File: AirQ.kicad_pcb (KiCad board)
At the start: 2 copper layers, 1 part, among them U1 ESP32-H2-MINI-1-H2

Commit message: changes
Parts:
- added D1: SS12, Diode_SMD:D_SMA, F.Cu at (130.0, 106.5)
- added U2: AP2112K-3.3, Package_TO_SOT_SMD:SOT-23-5, F.Cu at (139.2, 116.1)
- added U3: AP2112K-1.8, Package_TO_SOT_SMD:SOT-23-5, F.Cu at (128.5, 115.8)
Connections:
- U1 pad 1: unconnected-(U1-GND-Pad1) -> GND
- U1 pad 11: unconnected-(U1-GND-Pad11) -> GND
- U1 pad 14: unconnected-(U1-GND-Pad14) -> GND
- U1 pad 2: unconnected-(U1-GND-Pad2) -> GND
- U1 pad 25: unconnected-(U1-IO25-Pad25) -> D+
- U1 pad 26: unconnected-(U1-IO26-Pad26) -> D-
- U1 pad 36: unconnected-(U1-GND-Pad36) -> GND
- U1 pad 37: unconnected-(U1-GND-Pad37) -> GND
- U1 pad 38: unconnected-(U1-GND-Pad38) -> GND
- U1 pad 39: unconnected-(U1-GND-Pad39) -> GND
- U1 pad 40: unconnected-(U1-GND-Pad40) -> GND
- U1 pad 41: unconnected-(U1-GND-Pad41) -> GND
- U1 pad 42: unconnected-(U1-GND-Pad42) -> GND
- U1 pad 43: unconnected-(U1-GND-Pad43) -> GND
- U1 pad 44: unconnected-(U1-GND-Pad44) -> GND
- U1 pad 45: unconnected-(U1-GND-Pad45) -> GND
- U1 pad 46: unconnected-(U1-GND-Pad46) -> GND
- U1 pad 47: unconnected-(U1-GND-Pad47) -> GND
- U1 pad 48: unconnected-(U1-GND-Pad48) -> GND
- U1 pad 50: unconnected-(U1-GND-Pad50) -> GND
- U1 pad 51: unconnected-(U1-GND-Pad51) -> GND
- U1 pad 52: unconnected-(U1-GND-Pad52) -> GND

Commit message: Avances Viernes
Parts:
- added C1: 1uF, Capacitor_SMD:C_0201_0603Metric, F.Cu at (173.5, 81.8)
- added C10: 0.1uF, Capacitor_SMD:C_0402_1005Metric, F.Cu at (183.4, 55.5)
- added C11: 0.1uF, Capacitor_SMD:C_0402_1005Metric, F.Cu at (174.4, 90.0)
- added C12: 0.1uF, Capacitor_SMD:C_0402_1005Metric, F.Cu at (191.6, 68.0)
- added C13: 10uF, Capacitor_SMD:C_0402_1005Metric, F.Cu at (192.0, 57.4)
- added C14: 0.1uF, Capacitor_SMD:C_0402_1005Metric, F.Cu at (167.7, 52.6)
- added C2: 10uF, Capacitor_SMD:C_0402_1005Metric, F.Cu at (169.9, 83.5)
- added C3: 0.1uF, Capacitor_SMD:C_0402_1005Metric, F.Cu at (169.9, 81.7)
- added C4: 1uF, Capacitor_SMD:C_0201_0603Metric, F.Cu at (183.6, 74.8)
- added C5: 1uF, Capacitor_SMD:C_0201_0603Metric, F.Cu at (180.8, 75.8)
- added C6: 1uF, Capacitor_SMD:C_0201_0603Metric, F.Cu at (189.4, 78.4)
- added C7: 1uF, Capacitor_SMD:C_0201_0603Metric, F.Cu at (180.8, 74.2)
- added C8: 1uF, Capacitor_SMD:C_0201_0603Metric, F.Cu at (190.7, 79.4)
- added C9: 0.1uF, Capacitor_SMD:C_0402_1005Metric, F.Cu at (180.2, 82.3)
- added D2: LED, LED_SMD:LED_0603_1608Metric, F.Cu at (184.2, 82.5)
- added D3: WS2812B, LED_SMD:LED_WS2812B_PLCC4_5.0x5.0mm_P3.2mm, F.Cu at (179.1, 54.4)
- added D4: WS2812B, LED_SMD:LED_WS2812B_PLCC4_5.0x5.0mm_P3.2mm, F.Cu at (196.1, 69.2)
- added D5: WS2812B, LED_SMD:LED_WS2812B_PLCC4_5.0x5.0mm_P3.2mm, F.Cu at (179.6, 91.2)
- added P1: USB_C_Plug_USB2.0, Connector_USB:USB_C_Receptacle_GCT_USB4105-xx-A_16P_TopMnt_Horizontal, F.Cu at (197.2, 78.9)
- added Q1: BSS138, Package_TO_SOT_SMD:SOT-23, F.Cu at (181.9, 63.3)
- added R1: 10K, Resistor_SMD:R_0402_1005Metric, F.Cu at (172.0, 83.7)
- added R10: 4.7K, Resistor_SMD:R_0805_2012Metric, F.Cu at (185.4, 53.5)
- added R11: 4.7K, Resistor_SMD:R_0805_2012Metric, F.Cu at (187.7, 57.0)
- added R12: 4.7K, Resistor_SMD:R_0805_2012Metric, F.Cu at (172.7, 55.7)
- added R13: 4.7K, Resistor_SMD:R_0805_2012Metric, F.Cu at (168.6, 55.7)
- added R2: 5.1K, Resistor_SMD:R_1206_3216Metric_Pad1.30x1.75mm_HandSolder, F.Cu at (188.9, 84.5)
- added R3: 5.1K, Resistor_SMD:R_1206_3216Metric_Pad1.30x1.75mm_HandSolder, F.Cu at (188.9, 88.7)
- added R4: 10K, Resistor_SMD:R_0402_1005Metric, F.Cu at (178.9, 71.3)
- added R5: 330, Resistor_SMD:R_0805_2012Metric, F.Cu at (185.1, 79.5)
- added R6: 10K, Resistor_SMD:R_0402_1005Metric, F.Cu at (178.5, 63.6)
- added R7: 10K, Resistor_SMD:R_0402_1005Metric, F.Cu at (180.2, 84.2)
- added R8: 10K, Resistor_SMD:R_0402_1005Metric, F.Cu at (183.7, 66.6)
- added R9: 470, Resistor_SMD:R_1206_3216Metric, F.Cu at (178.5, 59.0)
- added SW1: EN, Button_Switch_SMD:SW_Push_1P1T_NO_CK_KMR2, F.Cu at (177.0, 84.3)
- added SW2: EN, Button_Switch_SMD:SW_Push_1P1T_NO_CK_KMR2, F.Cu at (171.7, 63.4)
- added U4: ENS161-BLGM, ENS161:XDCR_ENS161-BLGM, F.Cu at (191.5, 54.1)
- U3: value AP2112K-1.8 -> ENS210; footprint Package_TO_SOT_SMD:SOT-23-5 -> Package_DFN_QFN:AMS_QFN-4-1EP_2x2mm_P0.95mm_EP0.7x1.6mm
- moved U3 75.5 mm to (170.6, 53.0)
- moved D1 68.1 mm to (187.5, 70.1), turned to -90 degrees
- moved U1 66.0 mm to (171.8, 74.0), turned to 90 degrees
- moved U2 62.0 mm to (182.4, 71.6), turned to 180 degrees
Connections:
- U1 pad 10: unconnected-(U1-IO01-Pad10) -> /SCL
- U1 pad 22: unconnected-(U1-IO08-Pad22) -> Net-(U1-IO08)
- U1 pad 23: unconnected-(U1-IO9-Pad23) -> /BOOT
- U1 pad 24: unconnected-(U1-IO22-Pad24) -> /LED_P
- U1 pad 25: D+ -> unconnected-(U1-IO25-Pad25)
- U1 pad 26: D- -> /D-
- U1 pad 27: unconnected-(U1-IO27-Pad27) -> /D+
- U1 pad 3: unconnected-(U1-3v3-Pad3) -> +3.3V
- U1 pad 49: unconnected-(U1-EPAD-Pad49) -> GND
- U1 pad 53: unconnected-(U1-GND-Pad53) -> GND
- U1 pad 8: unconnected-(U1-EN-Pad8) -> /RESET
- U1 pad 9: unconnected-(U1-IO0-Pad9) -> /SDA
- U3 pad 2: GND -> /SCL
- U3 pad 3: +3.3V -> /SDA
- U3 pad 4: unconnected-(U3-NC-Pad4) -> GND
- U3 pad 5: +1V8 -> GND
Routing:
- net GND: track 0.00 -> 60.8 mm, vias 0 -> 57
- net +5V: track 0.00 -> 58.8 mm, vias 0 -> 2
- net /SCL: track 0.00 -> 53.9 mm, vias 0 -> 2
- net /SDA: track 0.00 -> 52.8 mm, vias 0 -> 2
- net Net-(D4-DOUT): track 0.00 -> 35.2 mm
- net /D+: track 0.00 -> 27.1 mm, vias 0 -> 2
- net /D-: track 0.00 -> 27.1 mm, vias 0 -> 2
- net VBUS: track 0.00 -> 25.4 mm, vias 0 -> 2
- net Net-(D3-DOUT): track 0.00 -> 23.1 mm, vias 0 -> 2
- net +3.3V: track 0.00 -> 19.6 mm, vias 0 -> 19
- net /RESET: track 0.00 -> 16.2 mm
- net /BOOT: track 0.00 -> 14.6 mm, vias 0 -> 2
- net Net-(P1-CC): track 0.00 -> 12.1 mm
- net Net-(P1-VCONN): track 0.00 -> 10.6 mm, vias 0 -> 2
- net Net-(Q1-D): track 0.00 -> 8.65 mm
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- added copper zone on In2.Cu, net +3.3V
- added copper zone on B.Cu, net GND
- added copper zone on F.Cu, net GND
- added copper zone on In1.Cu, net GND
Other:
- board outline added: 44.9 x 45 mm
- copper layers 2 -> 4

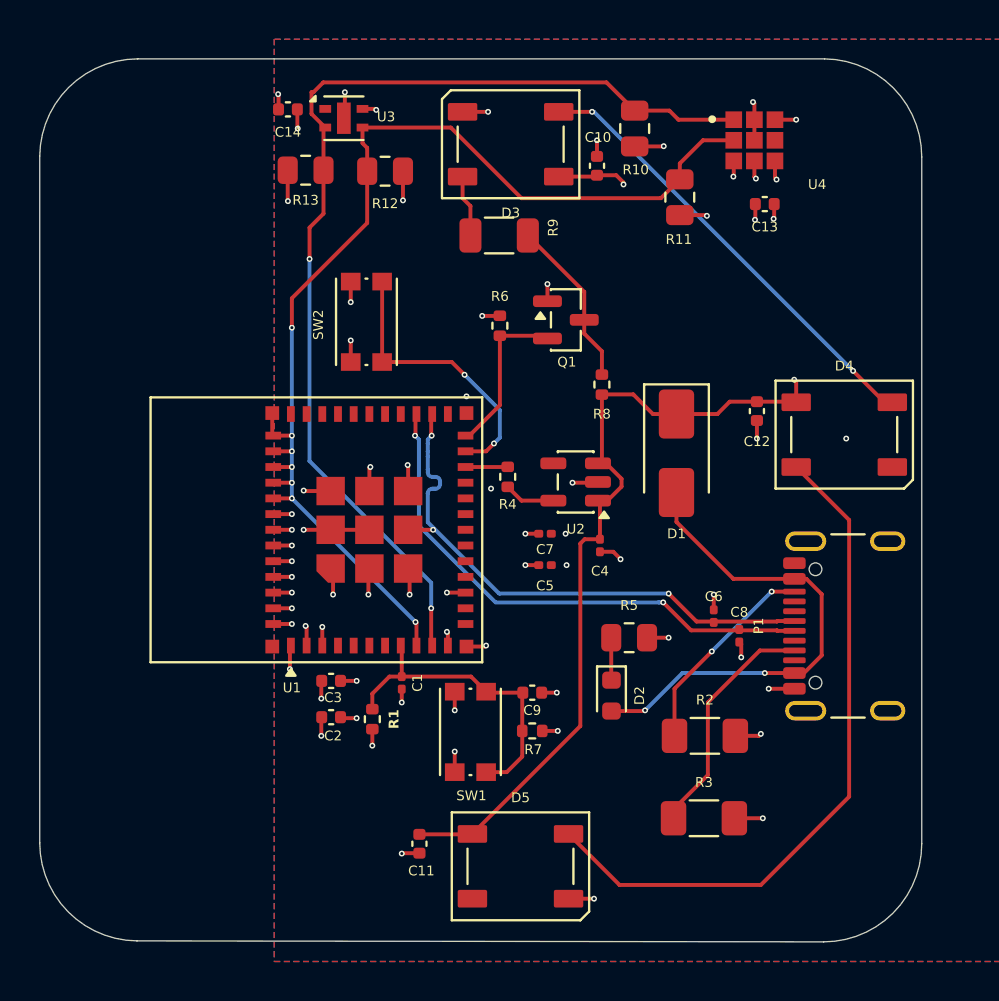
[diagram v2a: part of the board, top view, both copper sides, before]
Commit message: agujeros para la pcb
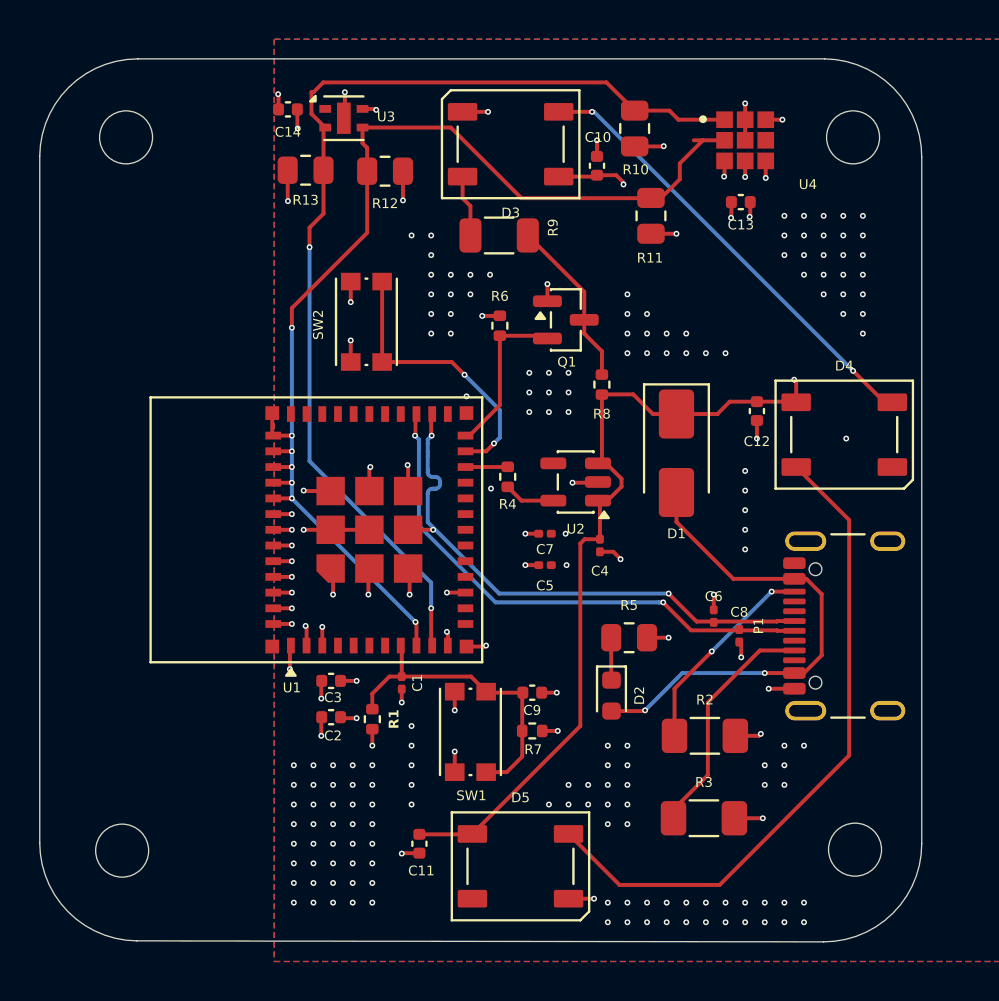
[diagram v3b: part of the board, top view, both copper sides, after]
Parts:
- added REF**: MountingHole_2.7mm_M2.5_DIN965, MountingHole:MountingHole_2.7mm_M2.5_DIN965, F.Cu at (196.6, 90.3)
- added REF**: MountingHole_2.7mm_M2.5_DIN965, MountingHole:MountingHole_2.7mm_M2.5_DIN965, F.Cu at (196.5, 54.0)
- added REF**: MountingHole_2.7mm_M2.5_DIN965, MountingHole:MountingHole_2.7mm_M2.5_DIN965, F.Cu at (159.2, 90.3)
- added REF**: MountingHole_2.7mm_M2.5_DIN965, MountingHole:MountingHole_2.7mm_M2.5_DIN965, F.Cu at (159.4, 54.0)
- moved R11 1.75 mm to (186.2, 58.0)
- moved C13 1.22 mm to (190.8, 57.3)
- moved U4 0.47 mm to (191.0, 54.1)
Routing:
- net Net-(D4-DOUT): track 35.2 -> 33.9 mm
- net +3.3V: track 19.6 -> 19.0 mm
- net GND: track 60.8 -> 60.7 mm, vias 57 -> 211
